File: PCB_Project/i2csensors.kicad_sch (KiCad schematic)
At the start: 0 parts

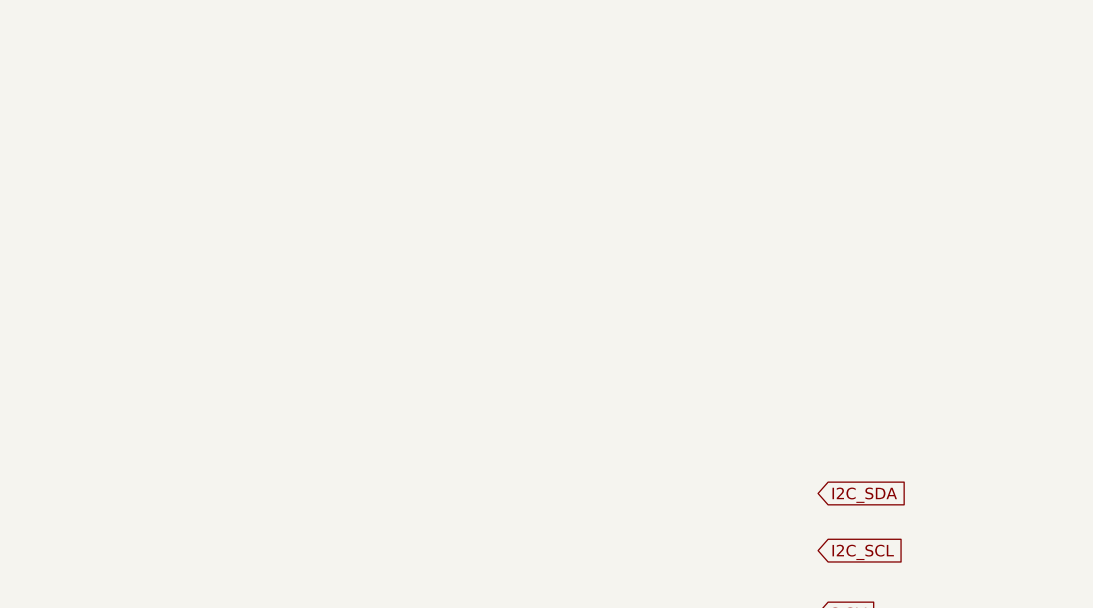
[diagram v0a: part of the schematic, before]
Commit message: First 2 i2c sensors
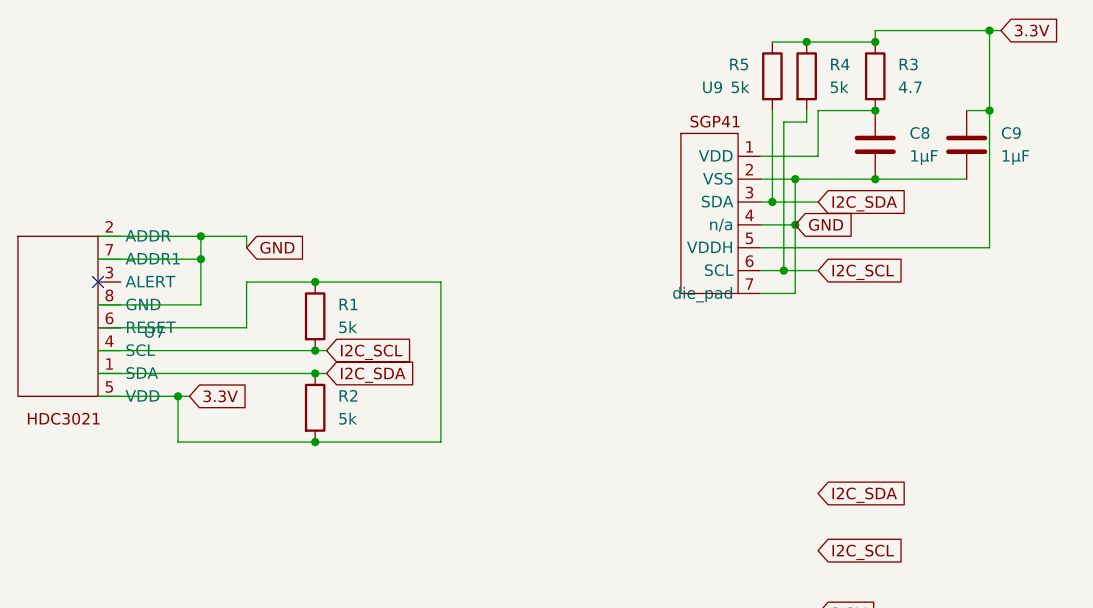
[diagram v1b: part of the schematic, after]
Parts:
- added C8, C9: 1µF, symbol Device:C
- added R1, R2, R4, R5: 5k, symbol Device:R
- added R3: 4.7, symbol Device:R
- added U7: ~, symbol sensors:HDC3021
- added U9: ~, symbol sensors:SGP41
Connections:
- net 3.3V: now also C9.1, R1.1, R2.2, R3.1, R4.1, R5.1, U7.5 (VDD), U7.6 (RESET), U9.5 (VDDH)
- net GND: now also C8.2, C9.2, U7.2 (ADDR), U7.7 (ADDR1), U7.8 (GND), U9.2 (VSS), U9.4 (n/a), U9.7 (die_pad)
- net I2C_SCL: now also R1.2, R4.2, U7.4 (SCL), U9.6 (SCL)
- net I2C_SDA: now also R2.1, R5.2, U7.1 (SDA), U9.3 (SDA)
- new net: C8.1, R3.2, U9.1 (VDD)
- no-connect marks 0 -> 1

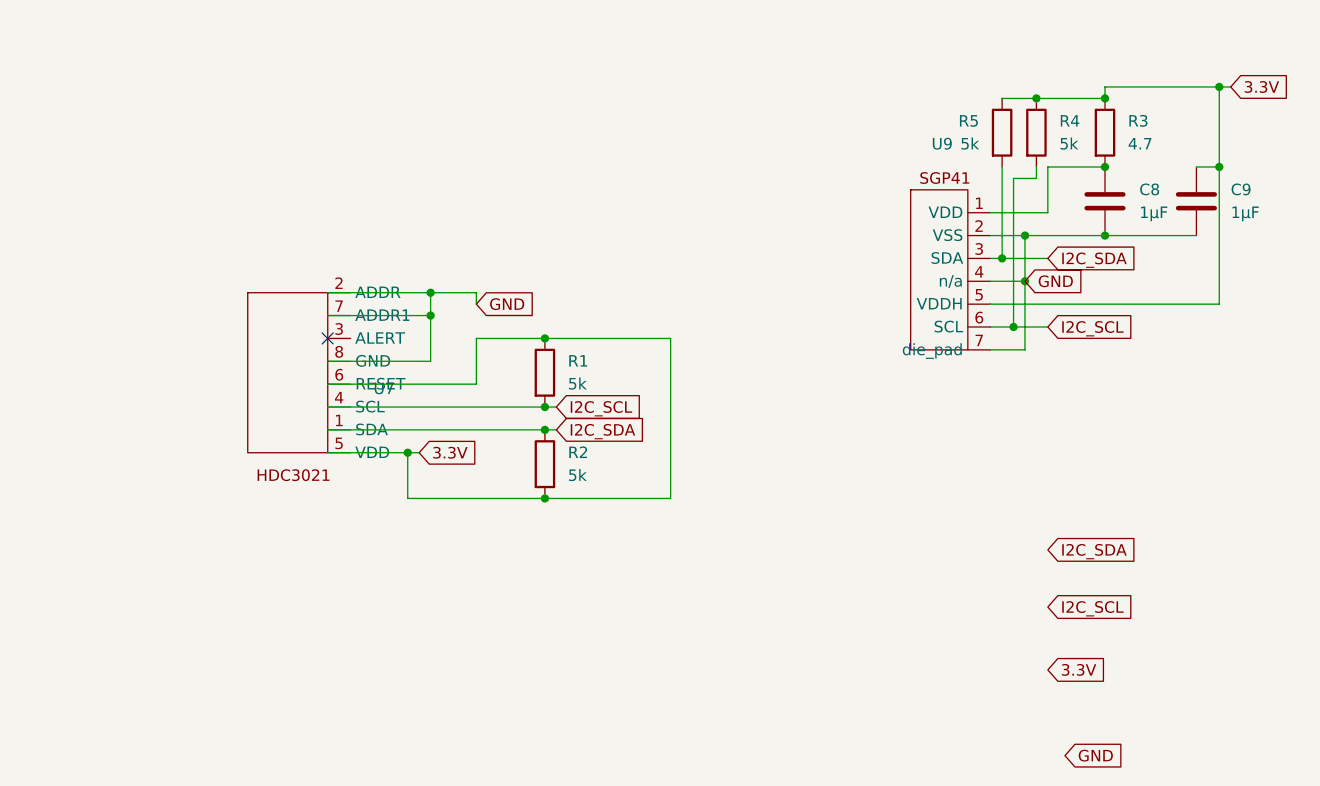
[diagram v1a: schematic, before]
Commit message: LIS3MDL and ELVH-015A-HNNJ-C-N2A4
bad version of the HDC3021QDEHRQ1 has been removed for now
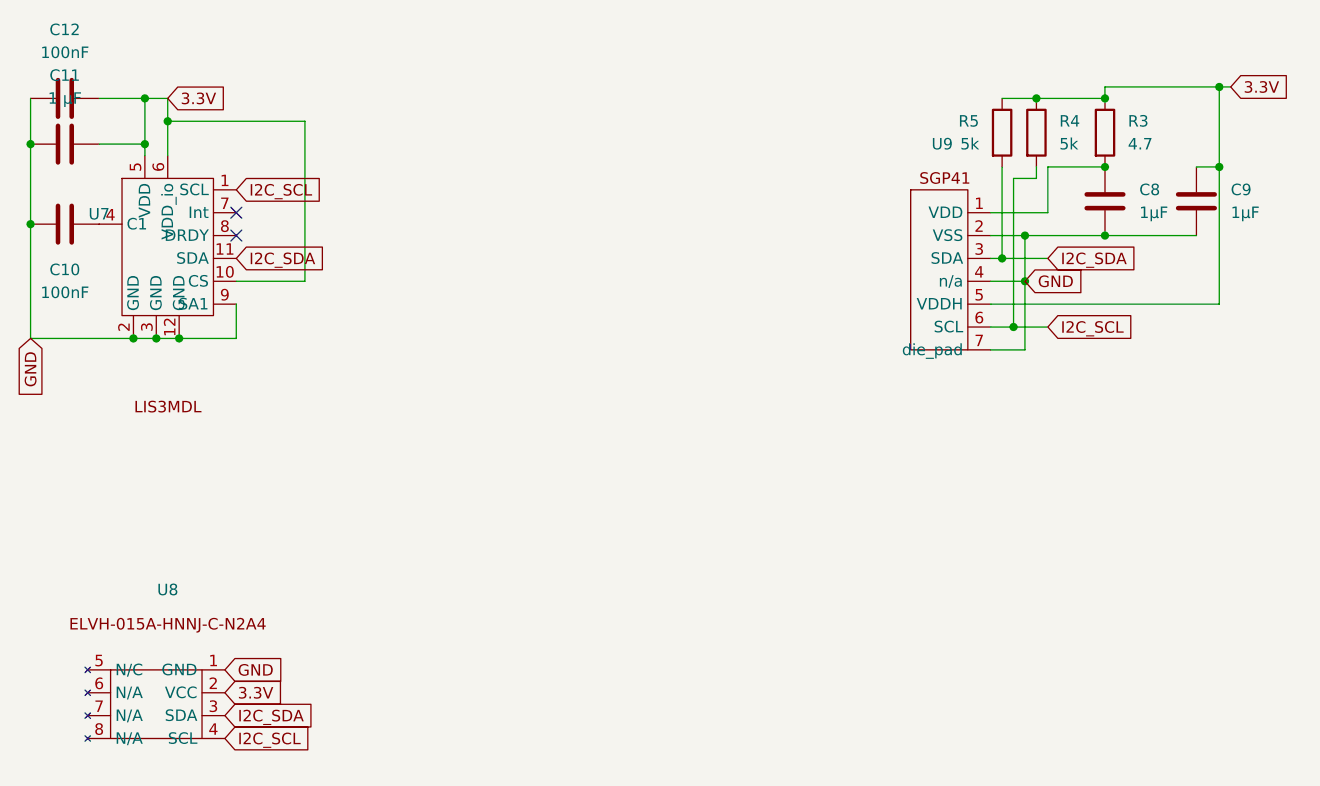
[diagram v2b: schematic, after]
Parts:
- removed R1, R2: 5k, symbol Device:R
- removed U7: ~, symbol sensors:HDC3021
- added C10, C12: 100nF, symbol Device:C
- added C11: 1 µF, symbol Device:C
- added U7: ~, symbol sensors:LIS3MDL
- added U8: ~, symbol sensors:ELVH-015A-HNNJ-C-N2A4
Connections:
- net 3.3V: now also C11.1, C12.1, U7.10 (CS), U7.5 (VDD), U7.6 (VDD_io), U8.2 (VCC)
- net GND: now also C10.2, C11.2, C12.2, U7.12 (GND), U7.2 (GND), U7.3 (GND), U7.9 (SA1), U8.1 (GND)
- net I2C_SCL: now also U7.1 (SCL), U8.4 (SCL)
- net I2C_SDA: now also U7.11 (SDA), U8.3 (SDA)
- new net: C10.1, U7.4 (C1)
- no-connect marks 1 -> 2

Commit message: I2C done
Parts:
- added C13: 0.1µF, symbol Device:C
- added R1, R2: 5k, symbol Device:R
- added R6, R7: 10K, symbol Device:R
- added U10: ~, symbol sensors:HDC3021
- added U11: ~, symbol sensors:ADT7410
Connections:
- net 3.3V: now also C13.1, R1.2, R2.2, R6.1, R7.1, U10.5 (VDD), U10.6 (RESET), U11.8 (VDD)
- net GND: now also C13.2, U10.2 (ADDR), U10.7 (ADDR1), U10.8 (GND), U11.3 (A0), U11.4 (A1), U11.7 (GND)
- net I2C_SCL: now also R2.1, R6.2, U10.4 (SCL), U11.1 (SCL)
- net I2C_SDA: now also R1.1, R7.2, U10.1 (SDA), U11.2 (SDA)
- no-connect marks 2 -> 5

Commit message: changed some symbols still going to clean up a bit
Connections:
- net 3.3V: no longer C13.1, C9.1, R1.2, R2.2, R3.1, R4.1, R5.1, R6.1, R7.1, U10.5 (VDD), U10.6 (RESET), U11.8 (VDD), U8.2 (VCC), U9.5 (VDDH)
- new net 3V3: C13.1, C9.1, R1.2, R2.2, R3.1, R4.1, R5.1, R6.1, R7.1, U10.5 (VDD), U10.6 (RESET), U11.8 (VDD), U8.2 (VCC), U9.5 (VDDH)

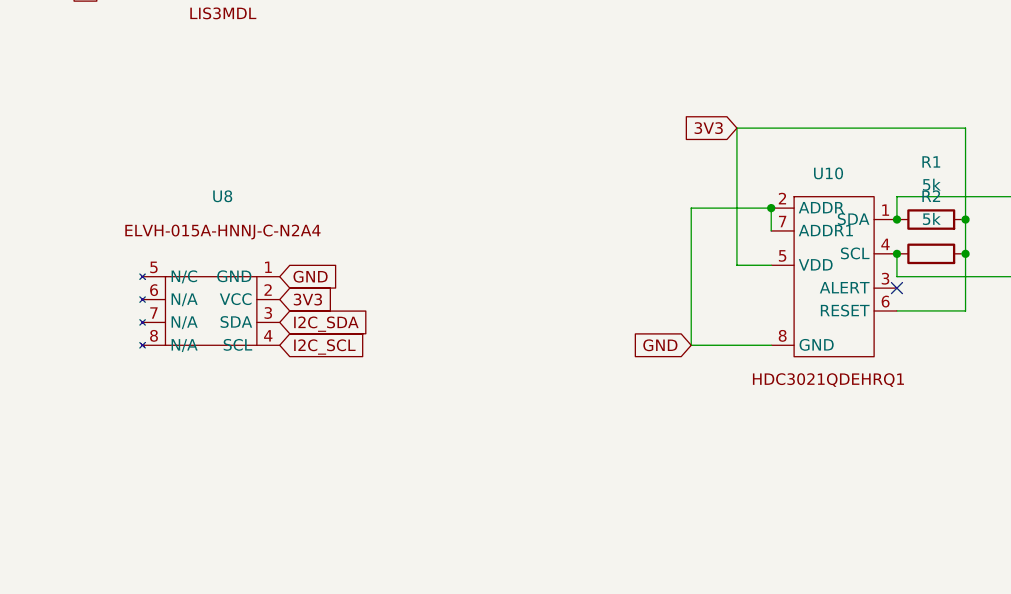
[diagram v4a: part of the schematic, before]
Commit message: added decumpiling caps
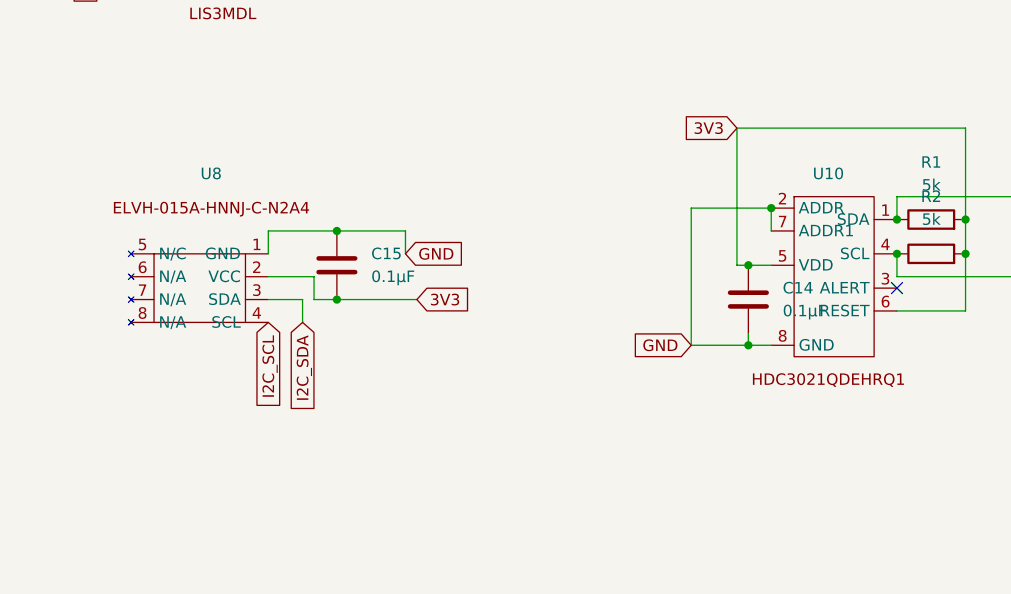
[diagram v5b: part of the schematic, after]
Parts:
- added C14, C15: 0.1µF, symbol Device:C
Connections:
- net 3V3: now also C14.1, C15.2
- net GND: now also C14.2, C15.1
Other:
- moved on the sheet: U8
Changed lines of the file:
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@@
   (junction (at 152.4 36.83) (diameter 0) (color 0 0 0 0)
   )
+  (junction (at 60.96 87.63) (diameter 0) (color 0 0 0 0)
+  )
   (junction (at 123.19 82.55) (diameter 0) (color 0 0 0 0)
   )
@@
   (junction (at 144.78 21.59) (diameter 0) (color 0 0 0 0)
   )
+  (junction (at 106.68 83.82) (diameter 0) (color 0 0 0 0)
+  )
   (junction (at 64.77 149.86) (diameter 0) (color 0 0 0 0)
   )
@@
   (junction (at 142.24 46.99) (diameter 0) (color 0 0 0 0)
   )
+  (junction (at 60.96 80.01) (diameter 0) (color 0 0 0 0)
+  )
   (junction (at 152.4 29.21) (diameter 0) (color 0 0 0 0)
   )
@@
   )
   (junction (at 44.45 48.26) (diameter 0) (color 0 0 0 0)
+  )
+  (junction (at 106.68 92.71) (diameter 0) (color 0 0 0 0)
   )
   (no_connect (at 55.88 34.29))
@@
     (stroke (width 0) (type default))
   )
+  (wire (pts (xy 58.42 85.09) (xy 58.42 87.63))
+    (stroke (width 0) (type default))
+  )
   (wire (pts (xy 139.7 34.29) (xy 146.05 34.29))
     (stroke (width 0) (type default))
@@
     (stroke (width 0) (type default))
   )
-  (wire (pts (xy 100.33 92.71) (xy 109.22 92.71))
+  (wire (pts (xy 100.33 92.71) (xy 106.68 92.71))
     (stroke (width 0) (type default))
   )
@@
     (stroke (width 0) (type default))
   )
+  (wire (pts (xy 60.96 87.63) (xy 69.85 87.63))
+    (stroke (width 0) (type default))
+  )
+  (wire (pts (xy 106.68 83.82) (xy 105.41 83.82))
+    (stroke (width 0) (type default))
+  )
   (wire (pts (xy 162.56 29.21) (xy 165.1 29.21))
     (stroke (width 0) (type default))
@@
     (stroke (width 0) (type default))
   )
+  (wire (pts (xy 53.34 87.63) (xy 57.15 87.63))
+    (stroke (width 0) (type default))
+  )
   (wire (pts (xy 48.26 24.13) (xy 48.26 27.94))
     (stroke (width 0) (type default))
@@
     (stroke (width 0) (type default))
   )
+  (wire (pts (xy 53.34 80.01) (xy 60.96 80.01))
+    (stroke (width 0) (type default))
+  )
   (wire (pts (xy 146.05 29.21) (xy 152.4 29.21))
     (stroke (width 0) (type default))
@@
     (stroke (width 0) (type default))
   )
+  (wire (pts (xy 60.96 80.01) (xy 68.58 80.01))
+    (stroke (width 0) (type default))
+  )
   (wire (pts (xy 152.4 36.83) (xy 143.51 36.83))
     (stroke (width 0) (type default))
@@
     (stroke (width 0) (type default))
   )
+  (wire (pts (xy 53.34 85.09) (xy 58.42 85.09))
+    (stroke (width 0) (type default))
+  )
   (wire (pts (xy 45.72 17.145) (xy 45.72 21.59))
     (stroke (width 0) (type default))
   )
+  (wire (pts (xy 57.15 87.63) (xy 57.15 90.17))
+    (stroke (width 0) (type default))
+  )
   (wire (pts (xy 48.26 24.13) (xy 68.58 24.13))
     (stroke (width 0) (type default))
@@
     (stroke (width 0) (type default))
   )
-  (wire (pts (xy 109.22 83.82) (xy 105.41 83.82))
+  (wire (pts (xy 109.22 83.82) (xy 106.68 83.82))
     (stroke (width 0) (type default))
   )
@@
     (stroke (width 0) (type default))
   )
+  (wire (pts (xy 68.58 80.01) (xy 68.58 82.55))
+    (stroke (width 0) (type default))
+  )
   (wire (pts (xy 165.1 44.45) (xy 165.1 29.21))
     (stroke (width 0) (type default))
@@
     (stroke (width 0) (type default))
   )
+  (wire (pts (xy 58.42 87.63) (xy 60.96 87.63))
+    (stroke (width 0) (type default))
+  )
   (wire (pts (xy 123.19 78.74) (xy 123.19 76.2))
     (stroke (width 0) (type default))
@@
     (stroke (width 0) (type default))
   )
+  (wire (pts (xy 53.34 80.01) (xy 53.34 82.55))
+    (stroke (width 0) (type default))
+  )
   (wire (pts (xy 109.22 77.47) (xy 109.22 80.01))
     (stroke (width 0) (type default))
@@
     (stroke (width 0) (type default))
   )
+  (wire (pts (xy 106.68 92.71) (xy 109.22 92.71))
+    (stroke (width 0) (type default))
+  )
   (wire (pts (xy 44.45 154.94) (xy 44.45 160.02))
     (stroke (width 0) (type default))
   )
+  (wire (pts (xy 106.68 91.44) (xy 106.68 92.71))
+    (stroke (width 0) (type default))
+  )
   (global_label "GND" (shape input) (at 64.77 149.86 0) (fields_autoplaced)
     (effects (font (size 1.27 1.27)) (justify left))
@@
     )
   )
-  (global_label "I2C_SDA" (shape input) (at 54.61 90.17 0) (fields_autoplaced)
-    (effects (font (size 1.27 1.27)) (justify left))
-    (property "Intersheetrefs" "${INTERSHEET_REFS}" (at 65.1358 90.17 0)
-      (effects (font (size 1.27 1.27)) (justify left) hide)
+  (global_label "I2C_SDA" (shape input) (at 57.15 90.17 270) (fields_autoplaced)
+    (effects (font (size 1.27 1.27)) (justify right))
+    (property "Intersheetrefs" "${INTERSHEET_REFS}" (at 57.15 100.7752 90)
+      (effects (font (size 1.27 1.27)) (justify right) hide)
     )
   )
@@
     )
   )
-  (global_label "I2C_SCL" (shape input) (at 54.61 92.71 0) (fields_autoplaced)
-    (effects (font (size 1.27 1.27)) (justify left))
-    (property "Intersheetrefs" "${INTERSHEET_REFS}" (at 65.0753 92.71 0)
-      (effects (font (size 1.27 1.27)) (justify left) hide)
+  (global_label "I2C_SCL" (shape input) (at 53.34 90.17 270) (fields_autoplaced)
+    (effects (font (size 1.27 1.27)) (justify right))
+    (property "Intersheetrefs" "${INTERSHEET_REFS}" (at 53.34 100.7147 90)
+      (effects (font (size 1.27 1.27)) (justify right) hide)
     )
   )
@@
     )
   )
-  (global_label "GND" (shape input) (at 54.61 85.09 0) (fields_autoplaced)
-    (effects (font (size 1.27 1.27)) (justify left))
-    (property "Intersheetrefs" "${INTERSHEET_REFS}" (at 61.3863 85.09 0)
+  (global_label "GND" (shape input) (at 68.58 82.55 0) (fields_autoplaced)
+    (effects (font (size 1.27 1.27)) (justify left))
+    (property "Intersheetrefs" "${INTERSHEET_REFS}" (at 75.3563 82.55 0)
       (effects (font (size 1.27 1.27)) (justify left) hide)
     )
@@
     )
   )
-  (global_label "3V3" (shape input) (at 54.61 87.63 0) (fields_autoplaced)
-    (effects (font (size 1.27 1.27)) (justify left))
-    (property "Intersheetrefs" "${INTERSHEET_REFS}" (at 61.0234 87.63 0)
+  (global_label "3V3" (shape input) (at 69.85 87.63 0) (fields_autoplaced)
+    (effects (font (size 1.27 1.27)) (justify left))
+    (property "Intersheetrefs" "${INTERSHEET_REFS}" (at 76.2634 87.63 0)
       (effects (font (size 1.27 1.27)) (justify left) hide)
     )
@@
     )
   )
+  (symbol (lib_id "Device:C") (at 106.68 87.63 0) (unit 1)
+    (in_bom yes) (on_board yes) (dnp no) (fields_autoplaced)
+    (property "Reference" "C14" (at 110.49 86.36 0)
+      (effects (font (size 1.27 1.27)) (justify left))
+    )
+    (property "Value" "0.1µF" (at 110.49 88.9 0)
+      (effects (font (size 1.27 1.27)) (justify left))
+    )
+    (property "Footprint" "" (at 107.6452 91.44 0)
+      (effects (font (size 1.27 1.27)) hide)
+    )
+    (property "Datasheet" "~" (at 106.68 87.63 0)
+      (effects (font (size 1.27 1.27)) hide)
+    )
+    (pin "1")
+    (pin "2")
+    (instances
+      (project "PCB_Project"
+        (path "/3dbd20c6-0b48-4a74-89bd-dd4c54711bfb/1ccf5c87-aea1-46d5-9874-6b9c3decc43f"
+          (reference "C14") (unit 1)
+        )
+      )
+    )
+  )
   (symbol (lib_id "Device:C") (at 64.77 146.05 0) (unit 1)
     (in_bom yes) (on_board yes) (dnp no) (fields_autoplaced)
@@
     )
   )
-  (symbol (lib_id "sensors:ELVH-015A-HNNJ-C-N2A4") (at 43.18 93.98 0) (unit 1)
-    (in_bom yes) (on_board yes) (dnp no) (fields_autoplaced)
-    (property "Reference" "U8" (at 48.26 76.2 0)
-      (effects (font (size 1.27 1.27)))
-    )
-    (property "Value" "~" (at 43.18 93.98 0)
-      (effects (font (size 1.27 1.27)))
-    )
-    (property "Footprint" "" (at 43.18 93.98 0)
-      (effects (font (size 1.27 1.27)) hide)
-    )
-    (property "Datasheet" "" (at 43.18 93.98 0)
+  (symbol (lib_id "sensors:ELVH-015A-HNNJ-C-N2A4") (at 41.91 91.44 0) (unit 1)
+    (in_bom yes) (on_board yes) (dnp no) (fields_autoplaced)
+    (property "Reference" "U8" (at 46.99 73.66 0)
+      (effects (font (size 1.27 1.27)))
+    )
+    (property "Value" "~" (at 41.91 91.44 0)
+      (effects (font (size 1.27 1.27)))
+    )
+    (property "Footprint" "" (at 41.91 91.44 0)
+      (effects (font (size 1.27 1.27)) hide)
+    )
+    (property "Datasheet" "" (at 41.91 91.44 0)
       (effects (font (size 1.27 1.27)) hide)
     )
@@
         )
       )
+    )
+  )
+  (symbol (lib_id "Device:C") (at 60.96 83.82 0) (unit 1)
+    (in_bom yes) (on_board yes) (dnp no) (fields_autoplaced)
+    (property "Reference" "C15" (at 64.77 82.55 0)
+      (effects (font (size 1.27 1.27)) (justify left))
+    )
+    (property "Value" "0.1µF" (at 64.77 85.09 0)
+      (effects (font (size 1.27 1.27)) (justify left))
+    )
+    (property "Footprint" "" (at 61.9252 87.63 0)
+      (effects (font (size 1.27 1.27)) hide)
+    )
+    (property "Datasheet" "~" (at 60.96 83.82 0)
+      (effects (font (size 1.27 1.27)) hide)
+    )
+    (pin "1")
+    (pin "2")
+    (instances
+      (project "PCB_Project"
+        (path "/3dbd20c6-0b48-4a74-89bd-dd4c54711bfb/1ccf5c87-aea1-46d5-9874-6b9c3decc43f"
+          (reference "C15") (unit 1)
+        )
+      )

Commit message: clean up thx david!
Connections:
- net 3V3: now also C8.2, R2.1, R4.2; no longer R2.2, R4.1, U10.6 (RESET)
- net GND: now also C8.1; no longer C8.2, U10.7 (ADDR1)
- net I2C_SCL: now also R2.2, R4.1; no longer R2.1, R4.2
- net at R3.2, U9.1 (VDD): no longer C8.1
- no-connect marks 5 -> 7
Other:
- moved on the sheet: C10, C11, C12, C13, C14, C15, R1, R2, R6, R7, U10, U11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

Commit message: ADDR1 on the 3021 is not NC
it should be going to ground
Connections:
- net GND: now also U10.7 (ADDR1)
- no-connect marks 7 -> 6
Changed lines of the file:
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@@
   (junction (at 66.675 66.675) (diameter 0) (color 0 0 0 0)
+  )
+  (junction (at 213.36 114.3) (diameter 0) (color 0 0 0 0)
   )
   (junction (at 64.135 40.005) (diameter 0) (color 0 0 0 0)
@@
   (no_connect (at 231.14 121.92))
   (no_connect (at 75.565 55.245))
-  (no_connect (at 213.36 116.84))
   (no_connect (at 159.385 126.365))
   (no_connect (at 231.14 124.46))
@@
     (stroke (width 0) (type default))
   )
+  (wire (pts (xy 213.36 114.3) (xy 213.36 116.84))
+    (stroke (width 0) (type default))
+  )
